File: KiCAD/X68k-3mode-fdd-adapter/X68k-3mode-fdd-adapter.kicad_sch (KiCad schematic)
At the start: 79 parts, among them J101 4pin, J102 Conn_02x06_Odd_Even, J103 Conn_01x02, J104 Conn_01x04, J105 Conn_01x02, J106 Conn_02x17_Odd_Even, J107 Conn_02x17_Odd_Even, J108 Conn_02x17_Odd_Even, Q101 DTC143Z, Q102 2SC2712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

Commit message: フロントパネルを作り始めた
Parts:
- added J109: Conn_01x03, Connector_PinHeader_2.54mm:PinHeader_1x03_P2.54mm_Vertical, symbol Connector_Generic:Conn_01x03
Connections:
- net CONTROLLER_OPTION: now also J109.2 (Pin_2)
- net GND: now also J109.3 (Pin_3)
- net GP_ENABLE: now also J109.1 (Pin_1)
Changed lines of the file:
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@@
 	(wire
 		(pts
+			(xy 281.94 248.92) (xy 276.86 248.92)
+		)
+		(stroke
+			(width 0)
+			(type default)
+		)
+	)
+	(wire
+		(pts
 			(xy 243.84 55.88) (xy 243.84 62.23)
 		)
@@
 	(wire
 		(pts
+			(xy 274.32 251.46) (xy 274.32 248.92)
+		)
+		(stroke
+			(width 0)
+			(type default)
+		)
+	)
+	(wire
+		(pts
 			(xy 358.14 149.86) (xy 358.14 152.4)
 		)
@@
 	(wire
 		(pts
+			(xy 279.4 254) (xy 279.4 256.54)
+		)
+		(stroke
+			(width 0)
+			(type default)
+		)
+	)
+	(wire
+		(pts
 			(xy 199.39 22.86) (xy 171.45 22.86)
 		)
@@
 	(wire
 		(pts
+			(xy 276.86 248.92) (xy 276.86 254)
+		)
+		(stroke
+			(width 0)
+			(type default)
+		)
+	)
+	(wire
+		(pts
 			(xy 358.14 212.09) (xy 358.14 214.63)
 		)
@@
 	(wire
 		(pts
+			(xy 281.94 254) (xy 279.4 254)
+		)
+		(stroke
+			(width 0)
+			(type default)
+		)
+	)
+	(wire
+		(pts
 			(xy 69.85 78.74) (xy 69.85 72.39)
 		)
@@
 	(wire
 		(pts
+			(xy 274.32 248.92) (xy 256.54 248.92)
+		)
+		(stroke
+			(width 0)
+			(type default)
+		)
+	)
+	(wire
+		(pts
 			(xy 38.1 106.68) (xy 43.18 106.68)
 		)
@@
 	(wire
 		(pts
+			(xy 276.86 254) (xy 256.54 254)
+		)
+		(stroke
+			(width 0)
+			(type default)
+		)
+	)
+	(wire
+		(pts
 			(xy 148.59 113.03) (xy 148.59 114.3)
 		)
@@
 	(wire
 		(pts
+			(xy 281.94 251.46) (xy 274.32 251.46)
+		)
+		(stroke
+			(width 0)
+			(type default)
+		)
+	)
+	(wire
+		(pts
 			(xy 134.62 200.66) (xy 152.4 200.66)
 		)
@@
 	)
 	(symbol
+		(lib_id "Connector_Generic:Conn_01x03")
+		(at 287.02 251.46 0)
+		(unit 1)
+		(exclude_from_sim no)
+		(in_bom yes)
+		(on_board yes)
+		(dnp no)
+		(fields_autoplaced yes)
+		(property "Reference" "J109"
+			(at 289.56 250.1899 0)
+			(effects
+				(font
+					(size 1.27 1.27)
+				)
+				(justify left)
+			)
+		)
+		(property "Value" "Conn_01x03"
+			(at 289.56 252.7299 0)
+			(effects
+				(font
+					(size 1.27 1.27)
+				)
+				(justify left)
+			)
+		)
+		(property "Footprint" "Connector_PinHeader_2.54mm:PinHeader_1x03_P2.54mm_Vertical"
+			(at 287.02 251.46 0)
+			(effects
+				(font
+					(size 1.27 1.27)
+				)
+				(hide yes)
+			)
+		)
+		(property "Datasheet" "~"
+			(at 287.02 251.46 0)
+			(effects
+				(font
+					(size 1.27 1.27)
+				)
+				(hide yes)
+			)
+		)
+		(property "Description" "Generic connector, single row, 01x03, script generated (kicad-library-utils/schlib/autogen/connector/)"
+			(at 287.02 251.46 0)
+			(effects
+				(font
+					(size 1.27 1.27)
+				)
+				(hide yes)
+			)
+		)
+		(pin "1"
+		)
+		(pin "2"
+		)
+		(pin "3"
+		)
+		(instances
+			(project ""
+				(path "/13b3a4ee-84d6-44b3-962d-9cf7c36d7564"
+					(reference "J109")
+					(unit 1)
+				)
+			)
+		)
+	)
+	(symbol
 		(lib_id "Device:R_Small_US")
 		(at 44.45 226.06 270)
@@
 					(unit 1)
 				)
+			)
+		)
+	)
+	(symbol
+		(lib_id "power:GND")
+		(at 279.4 256.54 0)
+		(unit 1)
+		(exclude_from_sim no)
+		(in_bom yes)
+		(on_board yes)
+		(dnp no)
+		(fields_autoplaced yes)
+		(property "Reference" "#PWR0169"
+			(at 279.4 262.89 0)
+			(effects
+				(font
+					(size 1.27 1.27)
+				)
+				(hide yes)
+			)
+		)
+		(property "Value" "GND"
+			(at 279.4 261.62 0)
+			(effects
+				(font
+					(size 1.27 1.27)
+				)
+			)
+		)
+		(property "Footprint" ""
+			(at 279.4 256.54 0)
+			(effects
+				(font
+					(size 1.27 1.27)
+				)
+				(hide yes)
+			)
+		)
+		(property "Datasheet" ""
+			(at 279.4 256.54 0)
+			(effects
+				(font
+					(size 1.27 1.27)
+				)
+				(hide yes)
+			)
+		)
+		(property "Description" "Power symbol creates a global label with name \"GND\" , ground"
+			(at 279.4 256.54 0)
+			(effects
+				(font
+					(size 1.27 1.27)
+				)
+				(hide yes)
+			)
+		)
+		(pin "1"
+		)
+		(instances
+			(project "X68k-3mode-fdd-adapter"
+				(path "/13b3a4ee-84d6-44b3-962d-9cf7c36d7564"
+					(reference "#PWR0169")
+					(unit 1)
+				)

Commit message: v2.0.1向けの修正を一通り入れたので一旦コミット
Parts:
- added D102: VDD MCU, Diode_SMD:D_0603_1608Metric_Pad1.05x0.95mm_HandSolder, symbol Device:LED
- added D103: +5V FDD, Diode_SMD:D_0603_1608Metric_Pad1.05x0.95mm_HandSolder, symbol Device:LED
- added D104: +12V FDD, Diode_SMD:D_0603_1608Metric_Pad1.05x0.95mm_HandSolder, symbol Device:LED
- added JP104, JP105, JP106: Jumper_2_Small_Open, Jumper:SolderJumper-2_P1.3mm_Open_RoundedPad1.0x1.5mm, symbol Jumper:Jumper_2_Small_Open
- added R129, R131: 1k, Resistor_SMD:R_0603_1608Metric, symbol Device:R_Small_US
- added R130: 10k, Resistor_SMD:R_0603_1608Metric, symbol Device:R_Small_US
- added R132, R134, R136: 3.3k, Resistor_SMD:R_0603_1608Metric, symbol Device:R_Small_US
- added R133, R135, R137: 0K, Resistor_SMD:R_0603_1608Metric, symbol Device:R_Small_US
- added SW103: BOOT, x68k-lib:SW_Push_TS1088R_02026, symbol Switch:SW_Push
- J101: footprint TerminalBlock_Phoenix:TerminalBlock_Phoenix_MPT-0,5-4-2.54_1x04_P2.54mm_Horizontal -> x68k-lib:TerminalBlock_WANJIE_WJ15EDGRC_1x04_P2.54mm_Horizontal
- SW102: footprint Button_Switch_SMD:SW_Push_SPST_NO_Alps_SKRK -> x68k-lib:SW_Push_TS1088R_02026
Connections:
- net +12V_FDD: now also D104.2 (A)
- net +5V_FDD: now also D103.2 (A)
- net GND: now also JP104.1 (A), JP105.1 (A), JP106.1 (A), R133.2, R135.2, R137.2; no longer J105.2 (Pin_2)
- net USB_D+: now also SW103.1
- net VDD_MCU: now also D102.2 (A), R129.1, R130.2
- net at J105.1 (Pin_1), Q101.1 (B): now also R130.1, R131.2
- new net: D104.1 (K), R136.1
- new net: R129.2, SW103.2
- new net: JP106.2 (B), R136.2, R137.1
- new net: D102.1 (K), R132.1
- new net: JP104.2 (B), R132.2, R133.1
- new net: D103.1 (K), R134.1
- new net: JP105.2 (B), R134.2, R135.1
- new net: J105.2 (Pin_2), R131.1
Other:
- moved on the sheet: H101, H102, H103, H104, H105, H106, H107, H108, H109, H110, J102, J103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

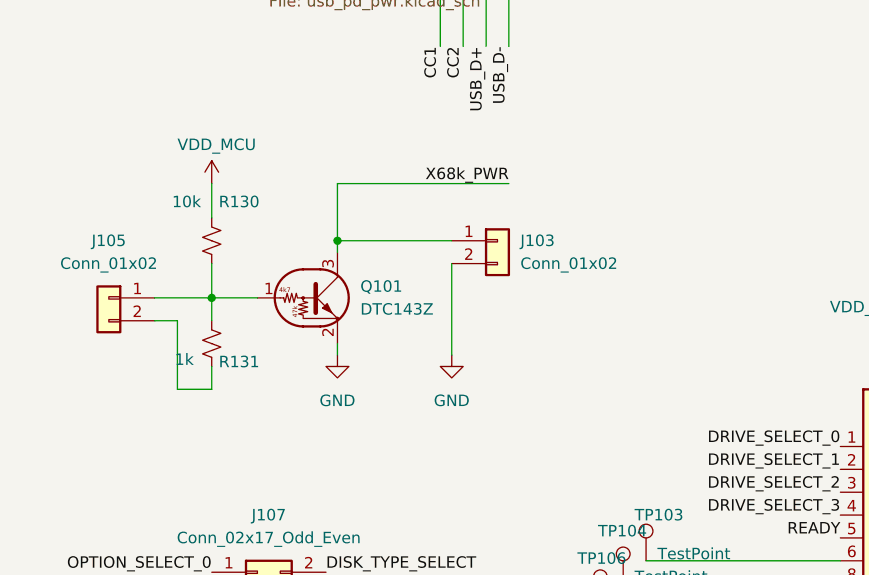
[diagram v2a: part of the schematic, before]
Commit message: 外部連動端子の回路のデジトラをFETに変更した
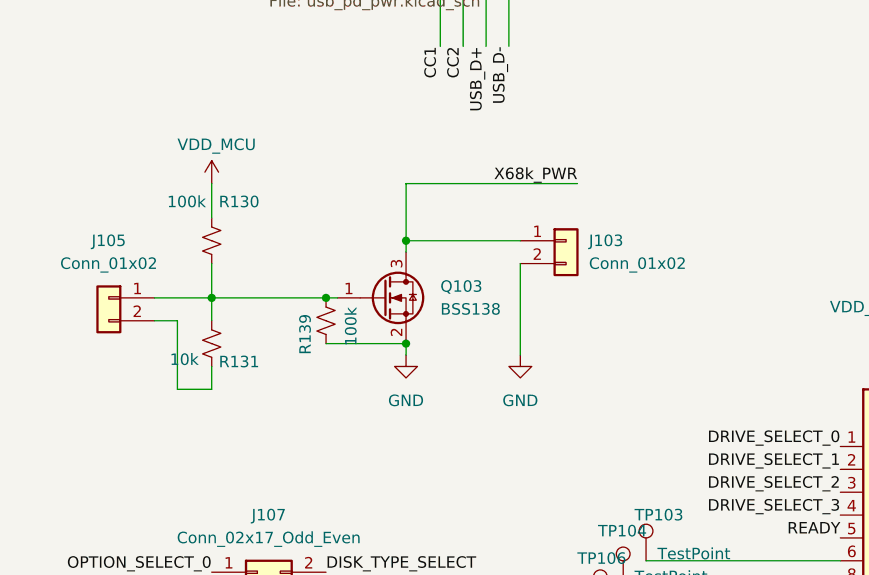
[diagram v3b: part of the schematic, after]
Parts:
- removed Q101: DTC143Z, Package_TO_SOT_SMD:SOT-523, symbol Transistor_BJT:DTC143Z
- added Q103: BSS138, Package_TO_SOT_SMD:SOT-23, symbol Transistor_FET:BSS138
- added R139: 100k, Resistor_SMD:R_0603_1608Metric, symbol Device:R_Small_US
- R130: value 10k -> 100k
- R131: value 1k -> 10k
- U102, U103, U105: LCSC (none) -> C3281959
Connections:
- net GND: now also Q103.2 (S), R139.1
- net X68k_PWR: now also Q103.3 (D)
- net at J105.1 (Pin_1), R130.1, R131.2: now also Q103.1 (G), R139.2
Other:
- moved on the sheet: J103

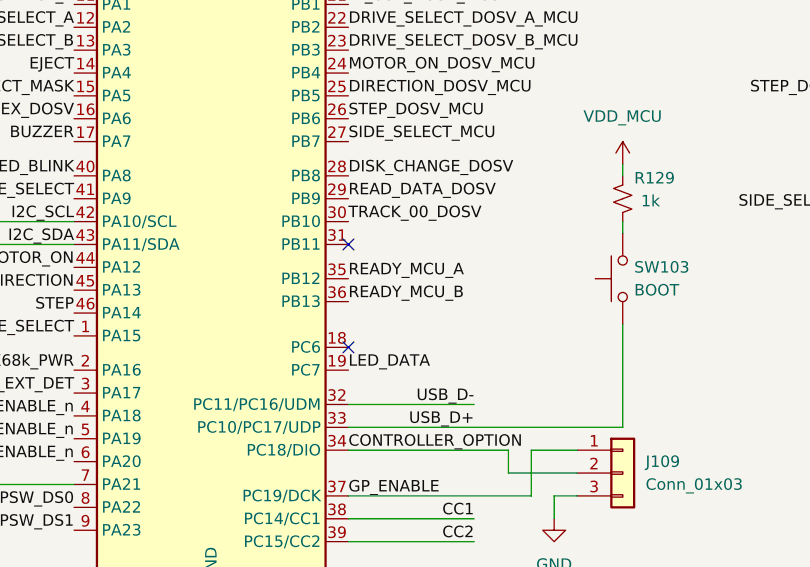
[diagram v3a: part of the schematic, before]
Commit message: 電源周りの回路を修正
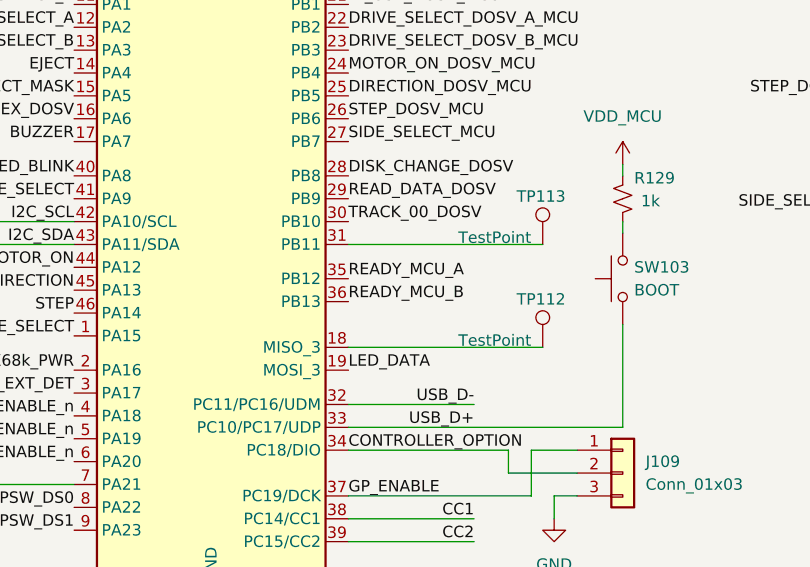
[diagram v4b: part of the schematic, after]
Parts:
- added TP112, TP113: TestPoint, TestPoint:TestPoint_Pad_1.0x1.0mm, symbol Connector:TestPoint
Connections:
- net at U104.18 (PC6): now also TP112.1
- net at U104.31 (PB11): now also TP113.1
- no-connect marks 12 -> 10

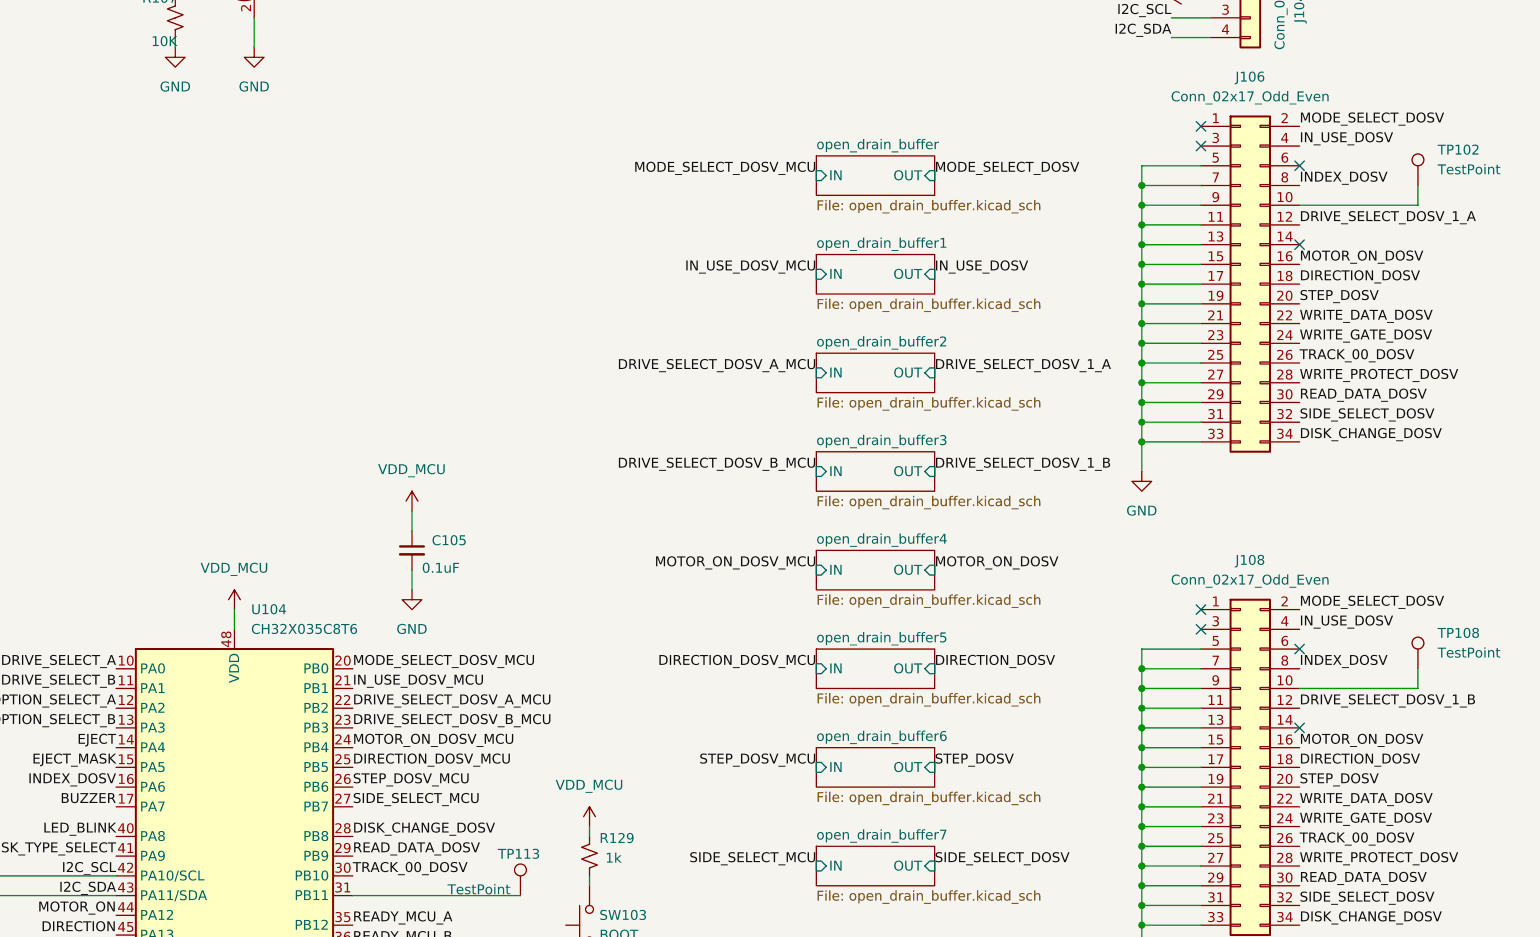
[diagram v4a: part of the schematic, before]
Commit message: * DCDCの出力の直後のダイオードをFETに変更 * DriveSelectのAとBが逆に配線されていた問題を修正
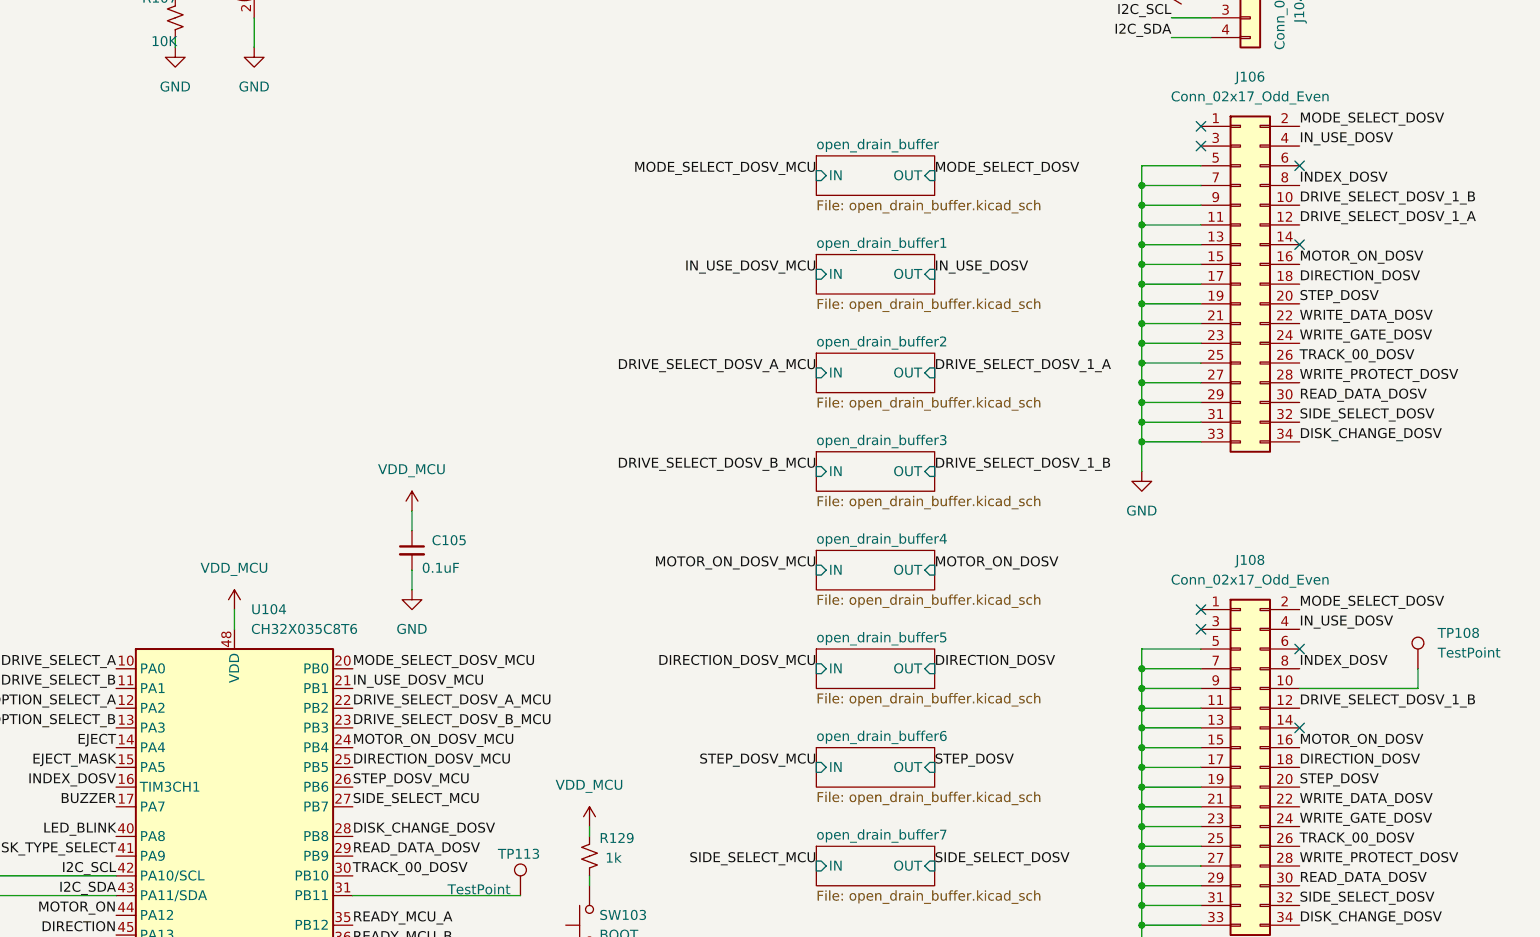
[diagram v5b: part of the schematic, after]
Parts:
- removed TP102: TestPoint, TestPoint:TestPoint_Pad_1.0x1.0mm, symbol Connector:TestPoint
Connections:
- net DRIVE_SELECT_DOSV_1_B: now also J106.10 (Pin_10)
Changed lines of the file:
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@@
 	(wire
 		(pts
-			(xy 393.7 137.16) (xy 393.7 134.62)
-		)
-		(stroke
-			(width 0)
-			(type default)
-		)
-	)
-	(wire
-		(pts
 			(xy 358.14 227.33) (xy 358.14 229.87)
 		)
@@
 	(wire
 		(pts
-			(xy 378.46 137.16) (xy 393.7 137.16)
-		)
-		(stroke
-			(width 0)
-			(type default)
-		)
-	)
-	(wire
-		(pts
 			(xy 46.99 215.9) (xy 59.69 215.9)
 		)
@@
 		)
 	)
+	(label "DRIVE_SELECT_DOSV_1_B"
+		(at 378.46 137.16 0)
+		(effects
+			(font
+				(size 1.27 1.27)
+			)
+			(justify left bottom)
+		)
+	)
 	(label "BUZZER"
 		(at 226.06 214.63 180)
@@
 		)
 		(pin "16"
+			(alternate "TIM3CH1")
 		)
 		(instances
@@
 					(unit 1)
 				)
-			)
-		)
-	)
-	(symbol
-		(lib_id "Connector:TestPoint")
-		(at 393.7 134.62 0)
-		(unit 1)
-		(exclude_from_sim no)
-		(in_bom yes)
-		(on_board yes)
-		(dnp no)
-		(fields_autoplaced yes)
-		(property "Reference" "TP102"
-			(at 396.24 130.0479 0)
-			(effects
-				(font
-					(size 1.27 1.27)
-				)
-				(justify left)
-			)
-		)
-		(property "Value" "TestPoint"
-			(at 396.24 132.5879 0)
-			(effects
-				(font
-					(size 1.27 1.27)
-				)
-				(justify left)
-			)
-		)
-		(property "Footprint" "TestPoint:TestPoint_Pad_1.0x1.0mm"
-			(at 398.78 134.62 0)
-			(effects
-				(font
-					(size 1.27 1.27)
-				)
-				(hide yes)
-			)
-		)
-		(property "Datasheet" "~"
-			(at 398.78 134.62 0)
-			(effects
-				(font
-					(size 1.27 1.27)
-				)
-				(hide yes)
-			)
-		)
-		(property "Description" "test point"
-			(at 393.7 134.62 0)
-			(effects
-				(font
-					(size 1.27 1.27)
-				)
-				(hide yes)
-			)
-		)
-		(property "LCIC" ""
-			(at 393.7 134.62 0)
-			(effects
-				(font
-					(size 1.27 1.27)
-				)
-				(hide yes)
-			)
-		)
-		(pin "1"
-		)
-		(instances
-			(project ""
-				(path "/13b3a4ee-84d6-44b3-962d-9cf7c36d7564"
-					(reference "TP102")
-					(unit 1)
-				)

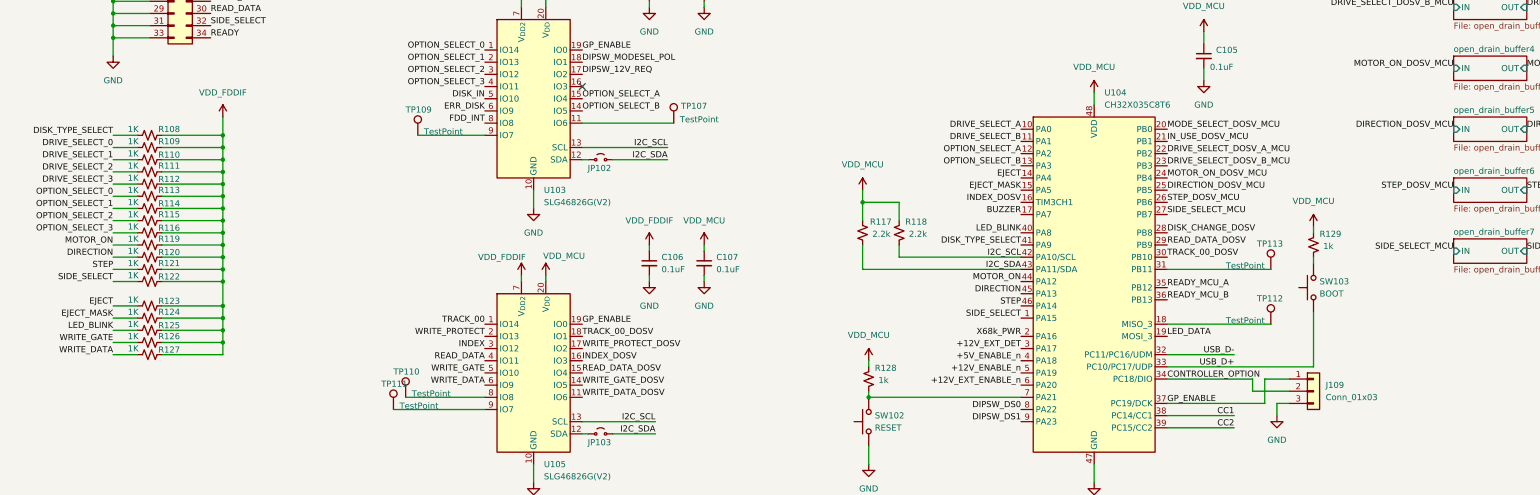
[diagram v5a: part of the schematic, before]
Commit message: * 9SCDRVの自動3モード切り替えができるようになった * OPTION_SELECTの配線が一つ増えたので回路も変更 (OPTION_SELECT_B_PAIR) * 2つのドライブで、1つは 1.2M、もう1つは1.44MBという状態でコピーに成功
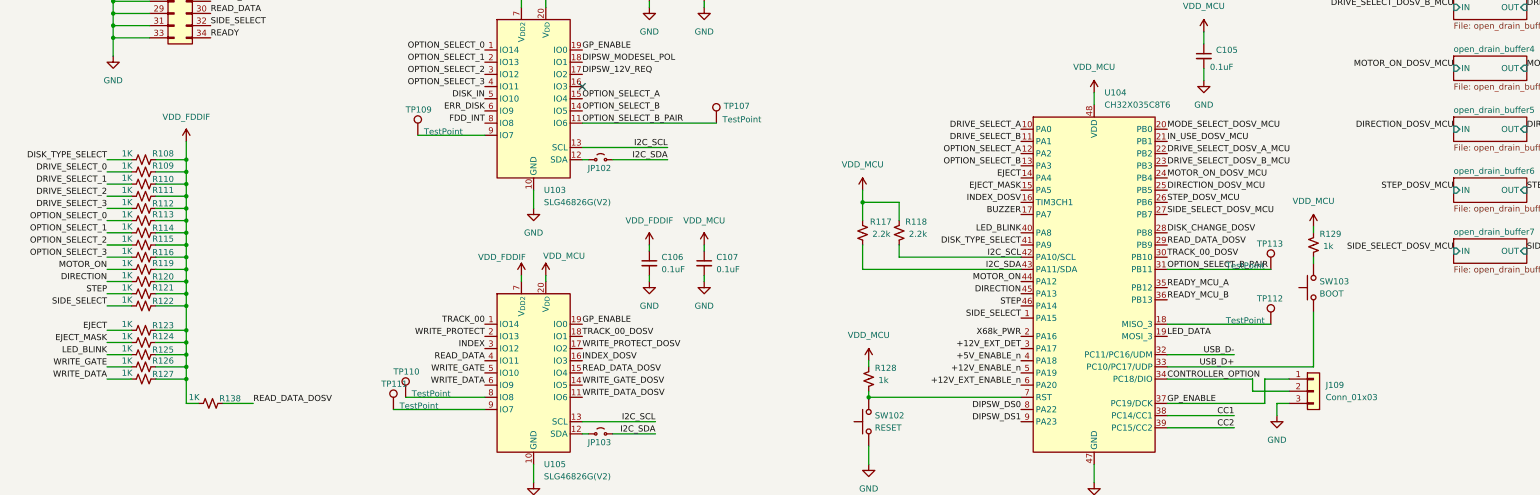
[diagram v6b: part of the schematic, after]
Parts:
- added R138: 1K, Resistor_SMD:R_0603_1608Metric, symbol Device:R_Small_US
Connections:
- net READ_DATA_DOSV: now also R138.1
- net VDD_FDDIF: now also R138.2
- net OPTION_SELECT_B_PAIR: now reaches TP113.1, U104.31 (PB11)
- net OPTION_SELECT_B_PAIR: now also TP107.1, U103.11 (IO6)
- net SIDE_SELECT_MCU renamed SIDE_SELECT_DOSV_MCU
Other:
- moved on the sheet: R108, R109, R110, R111, R112, R113, R114, R115, R116, R119, R120, R121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
